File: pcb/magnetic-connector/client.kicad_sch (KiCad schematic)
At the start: 8 parts

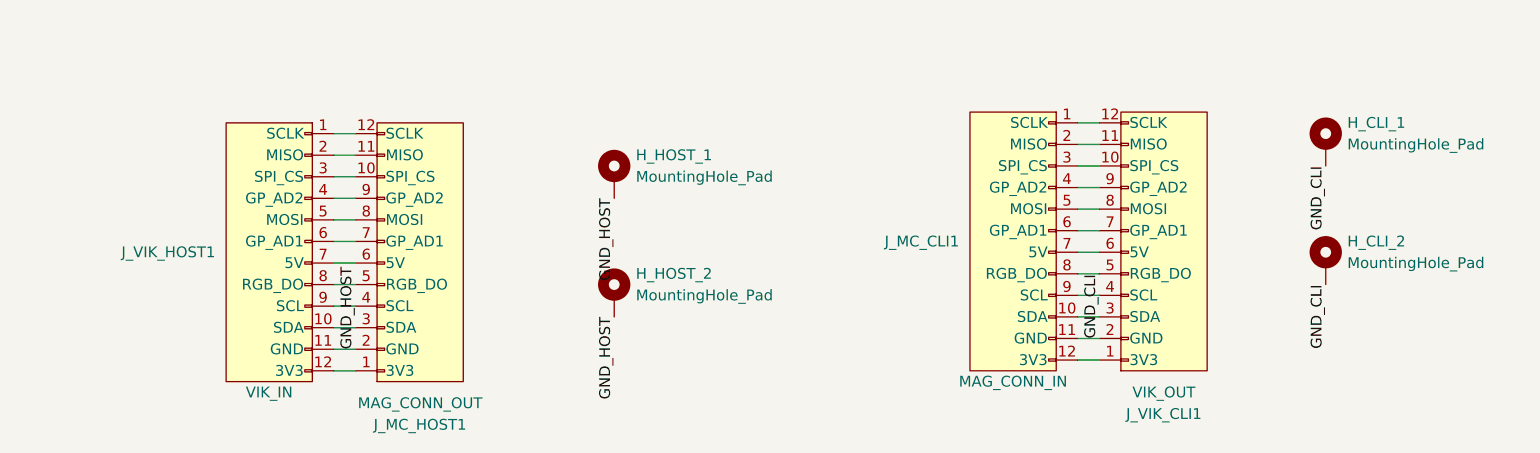
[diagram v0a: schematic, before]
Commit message: Make magnetic connector size compliant with VIK small form factor.
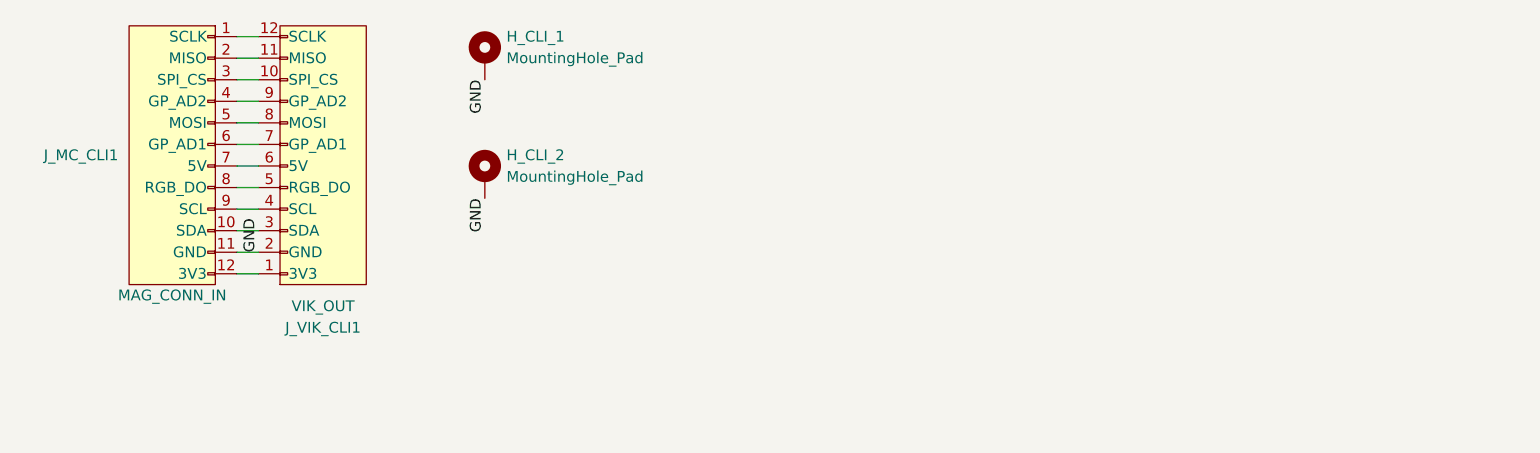
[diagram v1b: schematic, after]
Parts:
- removed H_HOST_1, H_HOST_2: MountingHole_Pad, MountingHole:MountingHole_2.2mm_M2_Pad, symbol Mechanical:MountingHole_Pad
- removed J_MC_HOST1: MAG_CONN_OUT, magnetic-connector:vik-keyboard-throughole-2.2mm, symbol vik:vik-keyboard-connector
- removed J_VIK_HOST1: VIK_IN, vik:vik-module-connector-vertical, symbol vik:vik-module-connector
- H_CLI_1, H_CLI_2: footprint MountingHole:MountingHole_2.2mm_M2_Pad -> MountingHole:MountingHole_2.2mm_M2MountingHole_MountingHole_2.2mm_M2
- J_MC_CLI1: footprint magnetic-connector:vik-module-throughole-2.2mm -> vik:vik-module-throughole-2.2mm
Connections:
- net GND_CLI renamed GND

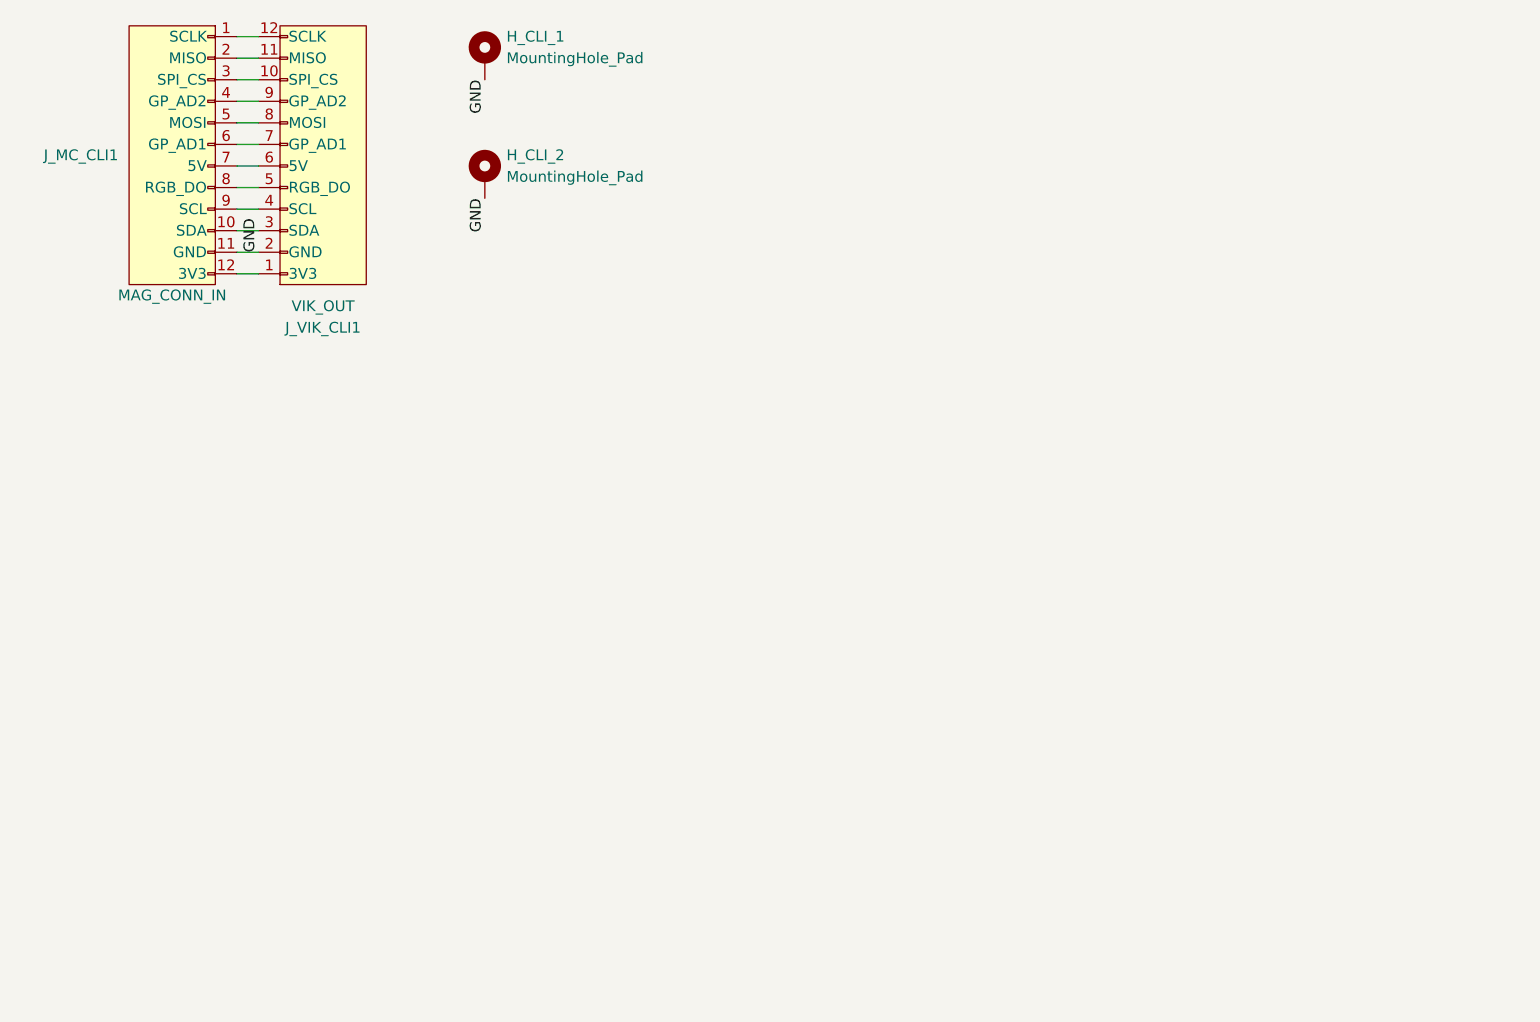
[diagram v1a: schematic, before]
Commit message: Add ESD protection to magnetic connector module.
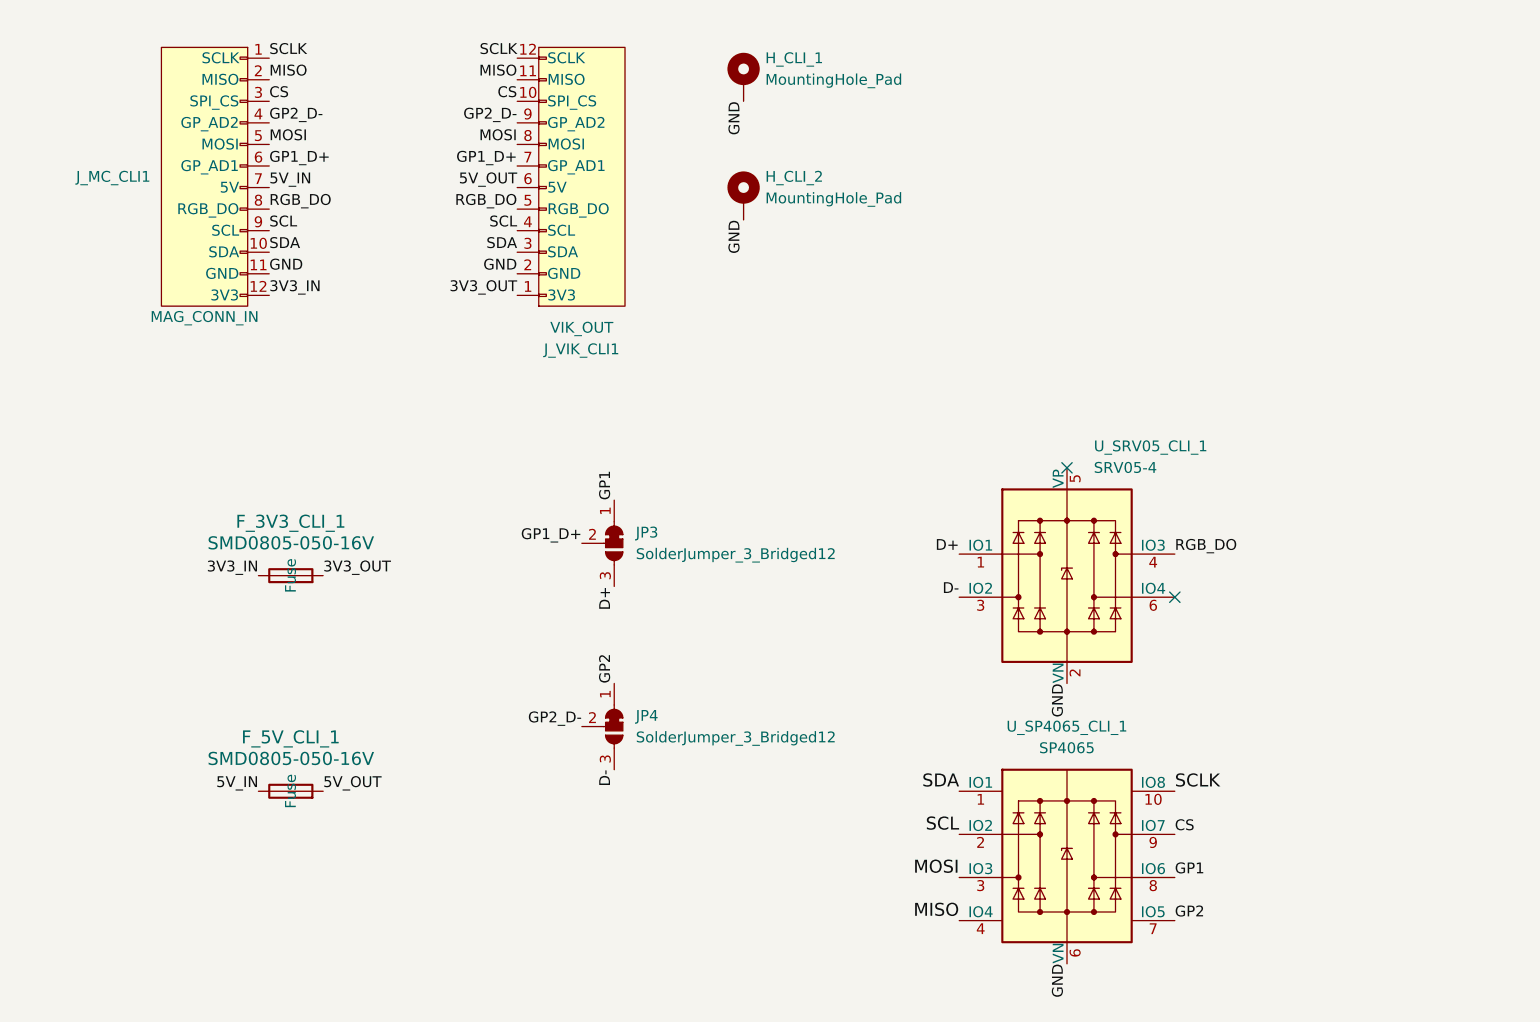
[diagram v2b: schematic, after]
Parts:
- added F_3V3_CLI_1, F_5V_CLI_1: SMD0805-050-16V, Fuse:Fuse_0805_2012Metric, symbol Device:Fuse
- added JP3, JP4: SolderJumper_3_Bridged12, Jumper:SolderJumper-3_P1.3mm_Bridged12_RoundedPad1.0x1.5mm_NumberLabels, symbol Jumper:SolderJumper_3_Bridged12
- added U_SP4065_CLI_1: SP4065, Package_SO:MSOP-10-1EP_3x3mm_P0.5mm_EP1.68x1.88mm, symbol SP4065:SP4065
- added U_SRV05_CLI_1: SRV05-4, Package_TO_SOT_SMD:SOT-23-6, symbol Power_Protection:SRV05-4
- H_CLI_1, H_CLI_2: footprint MountingHole:MountingHole_2.2mm_M2MountingHole_MountingHole_2.2mm_M2 -> MountingHole:MountingHole_2.2mm_M2_Pad
- J_MC_CLI1: footprint vik:vik-module-throughole-2.2mm -> magnetic-connector:vik-module-throughole-2.2mm
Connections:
- net GND: now also U_SP4065_CLI_1.6 (VN), U_SRV05_CLI_1.2 (VN)
- net SCLK: now reaches J_MC_CLI1.1 (SCLK), J_VIK_CLI1.12 (SCLK)
- net SCLK: now also U_SP4065_CLI_1.10 (IO8)
- net SDA: now reaches J_MC_CLI1.10 (SDA), J_VIK_CLI1.3 (SDA)
- net SDA: now also U_SP4065_CLI_1.1 (IO1)
- net 3V3_IN: now reaches J_MC_CLI1.12 (3V3)
- net 3V3_IN: now also F_3V3_CLI_1.1; no longer J_VIK_CLI1.1 (3V3)
- net MISO: now reaches J_MC_CLI1.2 (MISO), J_VIK_CLI1.11 (MISO)
- net MISO: now also U_SP4065_CLI_1.4 (IO4)
- net CS: now reaches J_MC_CLI1.3 (SPI_CS), J_VIK_CLI1.10 (SPI_CS)
- net CS: now also U_SP4065_CLI_1.9 (IO7)
- net GP2_D-: now reaches J_MC_CLI1.4 (GP_AD2), J_VIK_CLI1.9 (GP_AD2)
- net GP2_D-: now also JP4.2 (C)
- net MOSI: now reaches J_MC_CLI1.5 (MOSI), J_VIK_CLI1.8 (MOSI)
- net MOSI: now also U_SP4065_CLI_1.3 (IO3)
- net GP1_D+: now reaches J_MC_CLI1.6 (GP_AD1), J_VIK_CLI1.7 (GP_AD1)
- net GP1_D+: now also JP3.2 (C)
- net 5V_IN: now reaches J_MC_CLI1.7 (5V)
- net 5V_IN: now also F_5V_CLI_1.1; no longer J_VIK_CLI1.6 (5V)
- net RGB_DO: now reaches J_MC_CLI1.8 (RGB_DO), J_VIK_CLI1.5 (RGB_DO)
- net RGB_DO: now also U_SRV05_CLI_1.4 (IO3)
- net SCL: now reaches J_MC_CLI1.9 (SCL), J_VIK_CLI1.4 (SCL)
- net SCL: now also U_SP4065_CLI_1.2 (IO2)
- new net 3V3_OUT: F_3V3_CLI_1.2, J_VIK_CLI1.1 (3V3)
- new net 5V_OUT: F_5V_CLI_1.2, J_VIK_CLI1.6 (5V)
- new net D+: JP3.3 (B), U_SRV05_CLI_1.1 (IO1)
- new net D-: JP4.3 (B), U_SRV05_CLI_1.3 (IO2)
- new net GP1: JP3.1 (A), U_SP4065_CLI_1.8 (IO6)
- new net GP2: JP4.1 (A), U_SP4065_CLI_1.7 (IO5)
- no-connect marks 0 -> 2

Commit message: Change VIK connector and ESD protection chips.
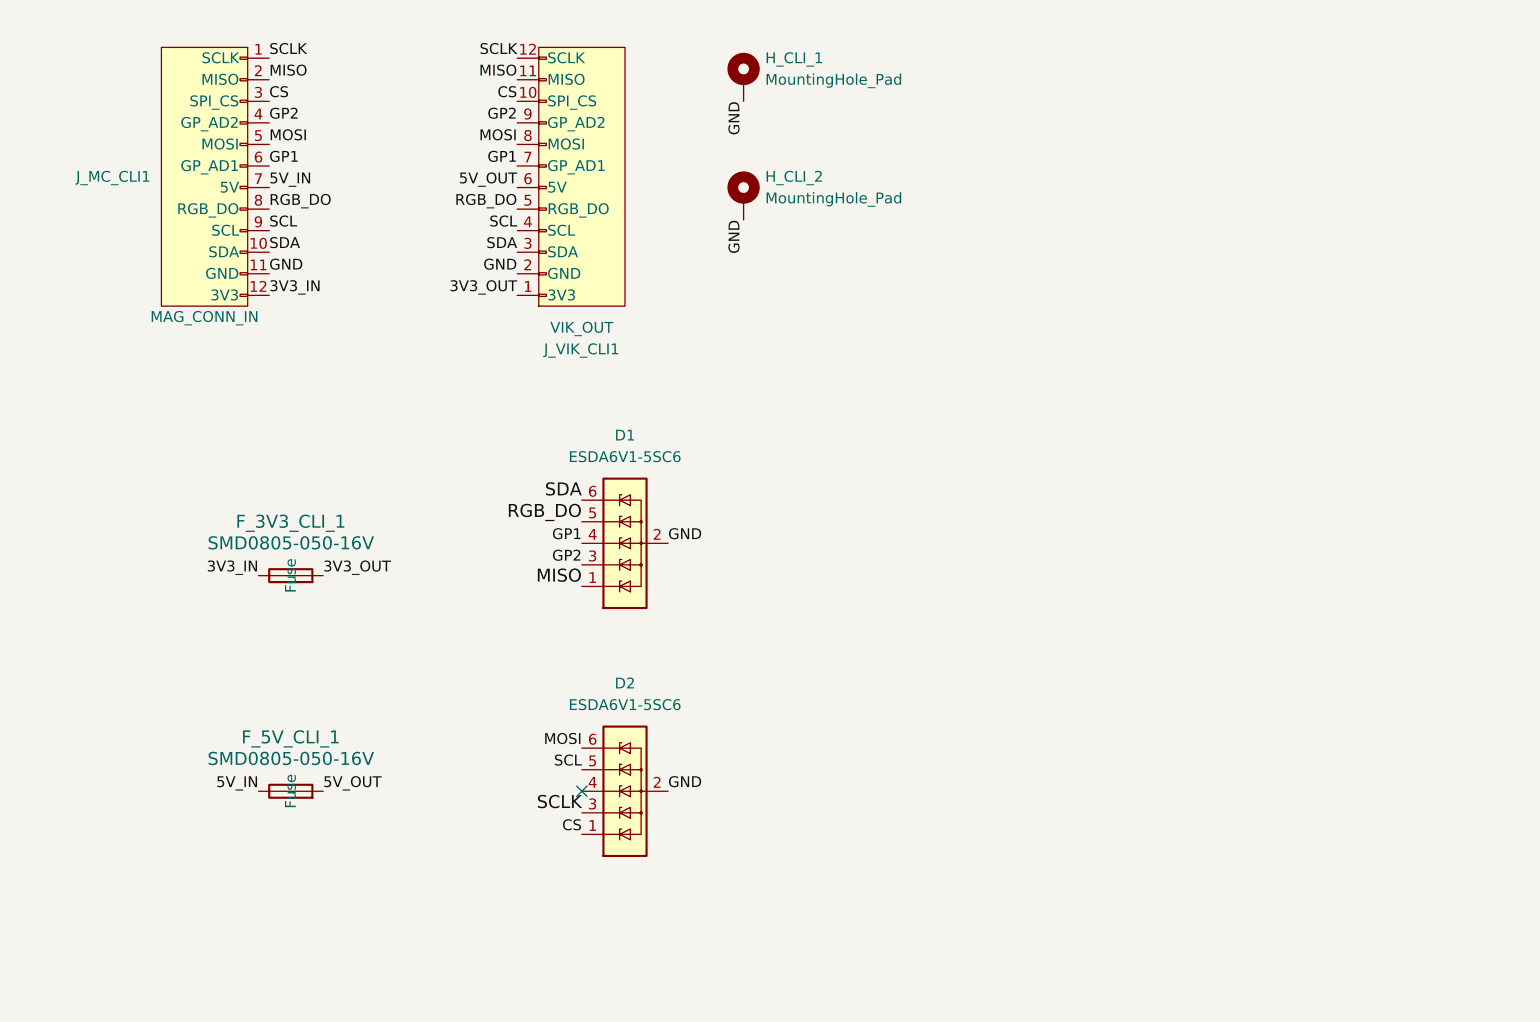
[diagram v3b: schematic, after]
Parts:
- removed JP3, JP4: SolderJumper_3_Bridged12, Jumper:SolderJumper-3_P1.3mm_Bridged12_RoundedPad1.0x1.5mm_NumberLabels, symbol Jumper:SolderJumper_3_Bridged12
- removed U_SP4065_CLI_1: SP4065, Package_SO:MSOP-10-1EP_3x3mm_P0.5mm_EP1.68x1.88mm, symbol SP4065:SP4065
- removed U_SRV05_CLI_1: SRV05-4, Package_TO_SOT_SMD:SOT-23-6, symbol Power_Protection:SRV05-4
- added D1, D2: ESDA6V1-5SC6, Package_TO_SOT_SMD:SOT-23-6, symbol Power_Protection:ESDA6V1-5SC6
- J_VIK_CLI1: footprint vik:vik-keyboard-connector-vertical -> vik:vik-keyboard-connector-horizontal
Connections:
- net GP1_D+ is gone; now on net GP1: J_MC_CLI1.6 (GP_AD1), J_VIK_CLI1.7 (GP_AD1)
- net GP2_D- is gone; now on net GP2: J_MC_CLI1.4 (GP_AD2), J_VIK_CLI1.9 (GP_AD2)
- net CS: now also D2.1 (IO1)
- net GND: now also D1.2 (GND), D2.2 (GND)
- net GP1: now also D1.4 (IO3)
- net GP2: now also D1.3 (IO2)
- net MISO: now also D1.1 (IO1)
- net MOSI: now also D2.6 (IO5)
- net RGB_DO: now also D1.5 (IO4)
- net SCL: now also D2.5 (IO4)
- net SCLK: now also D2.3 (IO2)
- net SDA: now also D1.6 (IO5)
- no-connect marks 2 -> 1
